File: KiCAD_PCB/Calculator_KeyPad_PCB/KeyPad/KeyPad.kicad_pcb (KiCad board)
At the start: 2 copper layers, 43 parts, among them J1 5034801000, SW1 SW_SPST, SW10 SW_SPST, SW11 SW_SPST, SW12 SW_SPST, SW13 SW_SPST, SW14 SW_SPST, SW15 SW_SPST, SW16 SW_SPST, SW17 SW_SPST, SW18 SW_SPST, SW19 SW_SPST, SW2 SW_SPST, SW20 SW_SPST, SW21 SW_SPST, SW3 SW_SPST, SW4 SW_SPST, SW5 SW_SPST, SW6 SW_SPST, SW7 SW_SPST, SW8 SW_SPST, SW9 SW_SPST

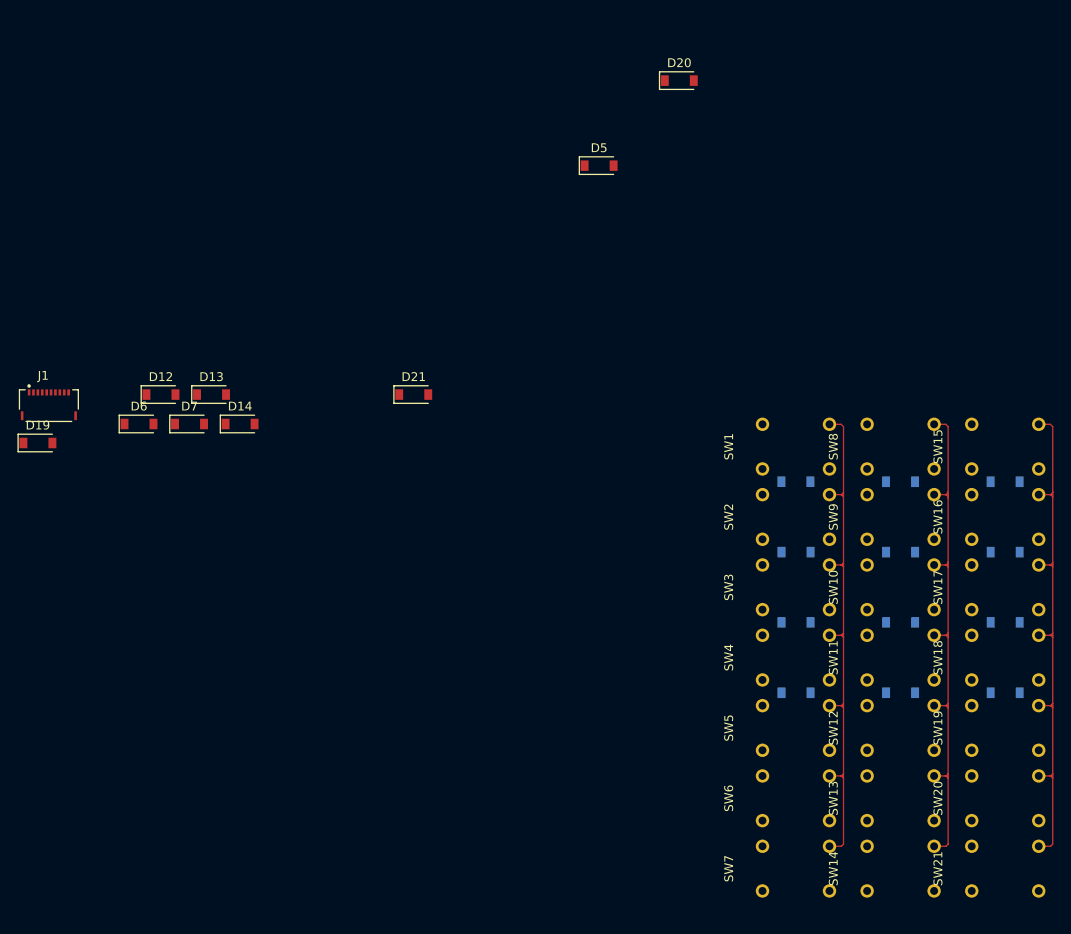
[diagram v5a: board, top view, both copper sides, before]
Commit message: PCB NumPad Updates
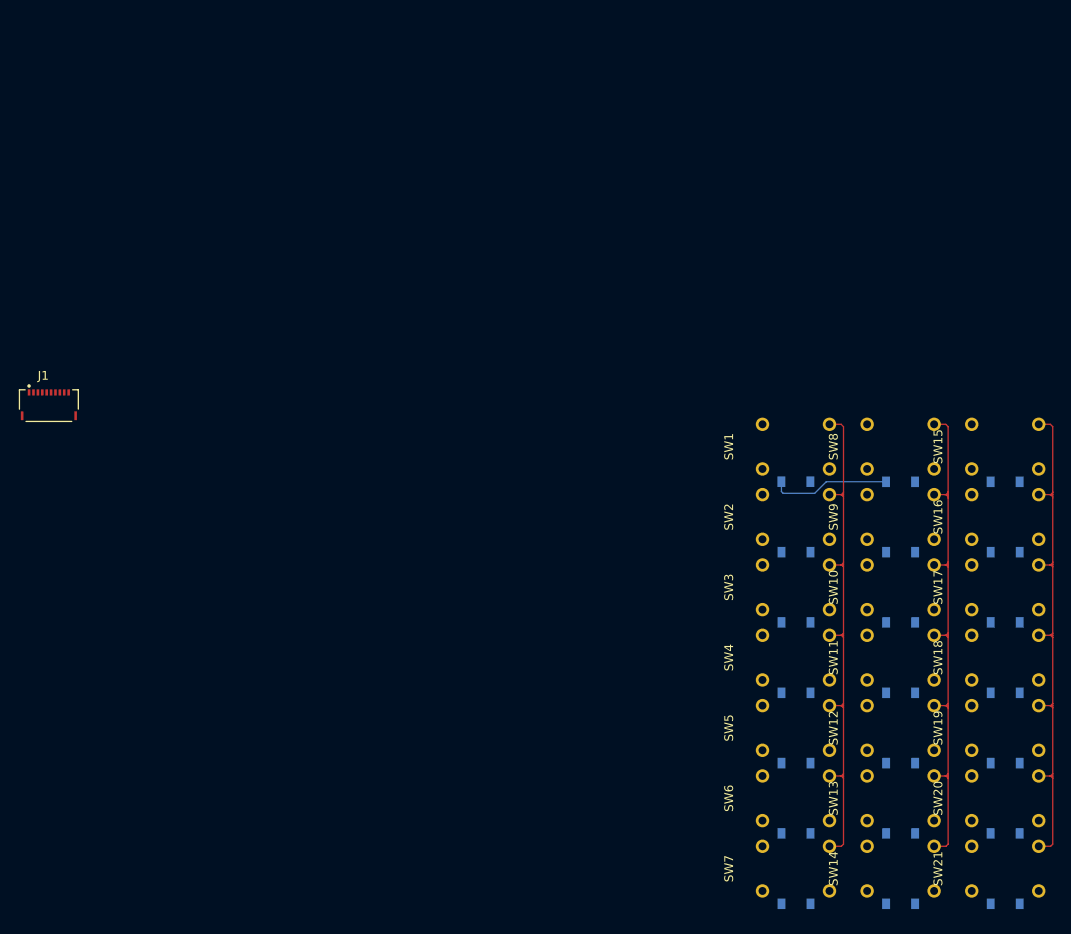
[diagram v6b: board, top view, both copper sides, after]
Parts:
- D12, D13, D14, D19, D20, D21, D5, D6, D7: moved to B.Cu
- moved D19 115.9 mm to (166.6, 108.0)
- moved D12 94.0 mm to (154.7, 108.0)
- moved D20 93.3 mm to (166.6, 116.0)
- moved D13 92.9 mm to (154.7, 116.0)
- moved D14 92.9 mm to (154.7, 124.0)
- moved D21 88.8 mm to (166.6, 124.0)
- moved D6 88.1 mm to (142.8, 116.0)
- moved D7 88.0 mm to (142.8, 124.0)
- moved D5 71.6 mm to (142.8, 108.0)
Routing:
- net /Row1: track 0.00 -> 13.7 mm

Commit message: NumPad PCB Updates
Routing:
- net /Row7: track 0.00 -> 27.4 mm
- net /Row6: track 0.00 -> 27.4 mm
- net /Row5: track 0.00 -> 27.4 mm
- net /Row4: track 0.00 -> 27.4 mm
- net /Row3: track 0.00 -> 27.4 mm
- net /Row2: track 0.00 -> 27.4 mm
- net /Row1: track 13.7 -> 27.4 mm

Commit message: NumPad Updates
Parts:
- moved J1 82.5 mm to (136.1, 92.0), turned to -90 degrees
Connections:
- J1 pad 1: /Row7 -> /Col15
- J1 pad 10: /Col15 -> /Row7
- J1 pad 2: /Row6 -> /Col14
- J1 pad 3: /Row5 -> /Col13
- J1 pad 4: /Row4 -> /Row1
- J1 pad 5: /Row3 -> /Row2
- J1 pad 6: /Row2 -> /Row3
- J1 pad 7: /Row1 -> /Row4
- J1 pad 8: /Col13 -> /Row5
- J1 pad 9: /Col14 -> /Row6
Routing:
- net Net-(D15-Pad2): track 0.00 -> 3.55 mm
- net Net-(D9-Pad2): track 0.00 -> 3.55 mm
- net Net-(D7-Pad2): track 0.00 -> 3.55 mm
- net Net-(D6-Pad2): track 0.00 -> 3.55 mm
- net Net-(D5-Pad2): track 0.00 -> 3.55 mm
- net Net-(D4-Pad2): track 0.00 -> 3.55 mm
- net Net-(D3-Pad2): track 0.00 -> 3.55 mm
- net Net-(D21-Pad2): track 0.00 -> 3.55 mm
- net Net-(D20-Pad2): track 0.00 -> 3.55 mm
- net Net-(D2-Pad2): track 0.00 -> 3.55 mm
- net Net-(D19-Pad2): track 0.00 -> 3.55 mm
- net Net-(D18-Pad2): track 0.00 -> 3.55 mm
- net Net-(D17-Pad2): track 0.00 -> 3.55 mm
- net Net-(D16-Pad2): track 0.00 -> 3.55 mm
- net Net-(D14-Pad2): track 0.00 -> 3.55 mm
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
